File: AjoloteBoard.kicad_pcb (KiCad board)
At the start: 2 copper layers, 69 x 84.9 mm, 10 parts, among them SW1 SW_Push_SPDT

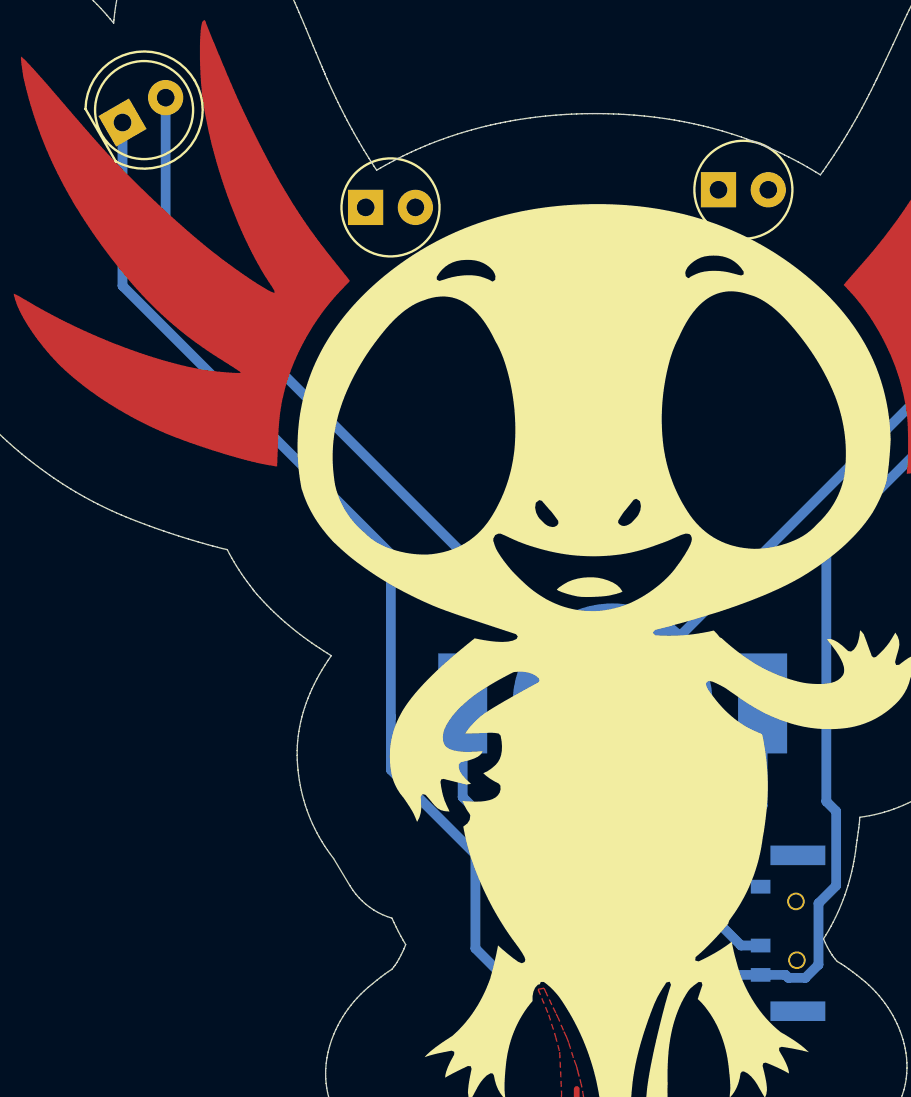
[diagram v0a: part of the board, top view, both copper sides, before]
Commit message: Update kicad version
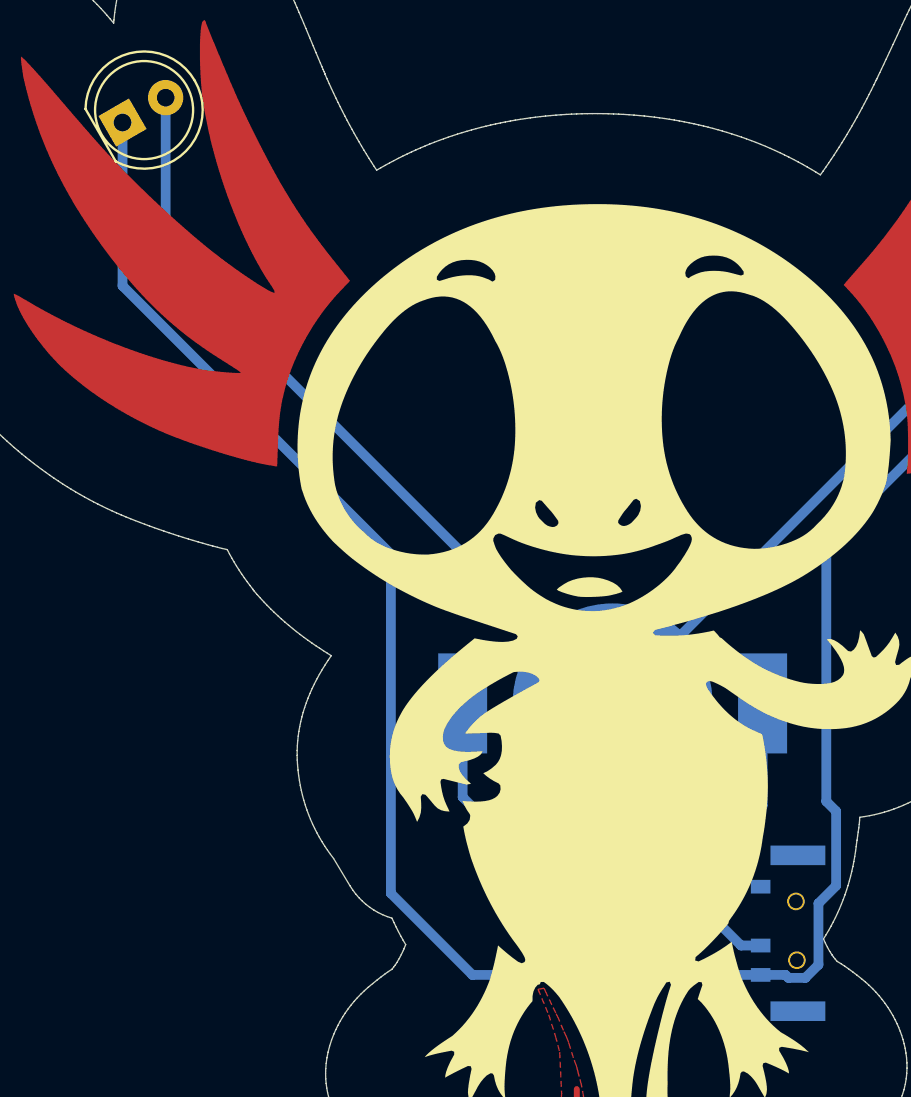
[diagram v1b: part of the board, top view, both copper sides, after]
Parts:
- removed the D1 at (147.2, 70.0)
- removed the D2 at (165.2, 69.1)
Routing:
- net Net-(D1-Pad1): track 116.7 -> 117.6 mm
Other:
- board text removed: "+"
- board text removed: "-"
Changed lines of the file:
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@@
-(kicad_pcb (version 4) (host pcbnew 4.0.7)
+(kicad_pcb (version 20171130) (host pcbnew "(5.0.0-3-g5ebb6b6)")
   (general
-    (links 0)
-    (no_connects 0)
-    (area 0 0 0 0)
     (thickness 1.6)
     (drawings 3)
-    (tracks 84)
+    (tracks 81)
     (zones 0)
     (modules 8)
@@
     (43 Eco2.User user)
     (44 Edge.Cuts user)
-    (45 Margin user hide)
+    (45 Margin user)
     (46 B.CrtYd user)
     (47 F.CrtYd user)
@@
       (layerselection 0x010f0_80000001)
       (usegerberextensions true)
+      (usegerberattributes false)
+      (usegerberadvancedattributes false)
+      (creategerberjobfile false)
       (excludeedgelayer true)
       (linewidth 0.100000)
@@
       (hpglpennumber 1)
       (hpglpenspeed 20)
-      (hpglpendiameter 15)
-      (hpglpenoverlay 2)
+      (hpglpendiameter 15.000000)
       (psnegative false)
       (psa4output false)
@@
       (drillshape 0)
       (scaleselection 1)
-      (outputdirectory /Volumes/Macintosh_HD/Documents/Electronic_Cats/Proyectos/Hw/WiFiTracker/AjoloteBoard/gerber/))
+      (outputdirectory "/Volumes/Macintosh_HD/Documents/Electronic_Cats/Proyectos/Hw/WiFiTracker/AjoloteBoard/gerber/"))
   )
   (net 0 "")
@@
     (add_net "Net-(SW1-Pad1)")
   )
-  (module LEDs:LED_D5.0mm (layer F.Cu)
-    (at 165.2 69.1)
-    (descr "LED, diameter 5.0mm, 2 pins, http://cdn-reichelt.de/documents/datenblatt/A500/LL-504BC2E-009.pdf")
-    (tags "LED diameter 5.0mm 2 pins")
-    (fp_text reference D2 (at 0.09 2.43) (layer B.SilkS)
-      (effects (font (size 1 1) (thickness 0.15)) (justify mirror))
-    )
-    (fp_text value LED (at 1.27 3.96) (layer F.Fab)
-      (effects (font (size 1 1) (thickness 0.15)))
-    )
-    (fp_arc (start 1.27 0) (end -1.23 -1.469694) (angle 299.1) (layer F.Fab) (width 0.1))
-    (fp_arc (start 1.27 0) (end -1.29 -1.54483) (angle 148.9) (layer F.Fab) (width 0.12))
-    (fp_arc (start 1.27 0) (end -1.29 1.54483) (angle -148.9) (layer F.Fab) (width 0.12))
-    (fp_circle (center 1.27 0) (end 3.77 0) (layer F.Fab) (width 0.1))
-    (fp_circle (center 1.27 0) (end 3.77 0) (layer F.SilkS) (width 0.12))
-    (fp_line (start -1.23 -1.469694) (end -1.23 1.469694) (layer F.Fab) (width 0.1))
-    (fp_line (start -1.29 -1.545) (end -1.29 1.545) (layer F.Fab) (width 0.12))
-    (fp_line (start -1.95 -3.25) (end -1.95 3.25) (layer F.CrtYd) (width 0.05))
-    (fp_line (start -1.95 3.25) (end 4.5 3.25) (layer F.CrtYd) (width 0.05))
-    (fp_line (start 4.5 3.25) (end 4.5 -3.25) (layer F.CrtYd) (width 0.05))
-    (fp_line (start 4.5 -3.25) (end -1.95 -3.25) (layer F.CrtYd) (width 0.05))
-    (fp_text user %R (at 1.25 0) (layer F.Fab)
-      (effects (font (size 0.8 0.8) (thickness 0.2)))
-    )
-    (pad 1 thru_hole rect (at 0 0) (size 1.8 1.8) (drill 0.9) (layers *.Cu *.Mask)
-      (net 2 "Net-(D1-Pad1)"))
-    (pad 2 thru_hole circle (at 2.54 0) (size 1.8 1.8) (drill 0.9) (layers *.Cu *.Mask)
-      (net 1 "Net-(BT1-Pad1)"))
-    (model ${KISYS3DMOD}/LEDs.3dshapes/LED_D5.0mm.wrl
-      (at (xyz 0 0 0))
-      (scale (xyz 0.393701 0.393701 0.393701))
-      (rotate (xyz 0 0 0))
-    )
-  )
-  (module LEDs:LED_D5.0mm (layer F.Cu)
-    (at 147.2 70)
-    (descr "LED, diameter 5.0mm, 2 pins, http://cdn-reichelt.de/documents/datenblatt/A500/LL-504BC2E-009.pdf")
-    (tags "LED diameter 5.0mm 2 pins")
-    (fp_text reference D1 (at 1.36 3.87) (layer B.SilkS)
-      (effects (font (size 1 1) (thickness 0.15)) (justify mirror))
-    )
-    (fp_text value LED (at 1.27 3.96) (layer F.Fab)
-      (effects (font (size 1 1) (thickness 0.15)))
-    )
-    (fp_arc (start 1.27 0) (end -1.23 -1.469694) (angle 299.1) (layer F.Fab) (width 0.1))
-    (fp_arc (start 1.27 0) (end -1.29 -1.54483) (angle 148.9) (layer F.Fab) (width 0.12))
-    (fp_arc (start 1.27 0) (end -1.29 1.54483) (angle -148.9) (layer F.Fab) (width 0.12))
-    (fp_circle (center 1.27 0) (end 3.77 0) (layer F.Fab) (width 0.1))
-    (fp_circle (center 1.27 0) (end 3.77 0) (layer F.SilkS) (width 0.12))
-    (fp_line (start -1.23 -1.469694) (end -1.23 1.469694) (layer F.Fab) (width 0.1))
-    (fp_line (start -1.29 -1.545) (end -1.29 1.545) (layer F.Fab) (width 0.12))
-    (fp_line (start -1.95 -3.25) (end -1.95 3.25) (layer F.CrtYd) (width 0.05))
-    (fp_line (start -1.95 3.25) (end 4.5 3.25) (layer F.CrtYd) (width 0.05))
-    (fp_line (start 4.5 3.25) (end 4.5 -3.25) (layer F.CrtYd) (width 0.05))
-    (fp_line (start 4.5 -3.25) (end -1.95 -3.25) (layer F.CrtYd) (width 0.05))
-    (fp_text user %R (at 1.25 0) (layer F.Fab)
-      (effects (font (size 0.8 0.8) (thickness 0.2)))
-    )
-    (pad 1 thru_hole rect (at 0 0) (size 1.8 1.8) (drill 0.9) (layers *.Cu *.Mask)
-      (net 2 "Net-(D1-Pad1)"))
-    (pad 2 thru_hole circle (at 2.54 0) (size 1.8 1.8) (drill 0.9) (layers *.Cu *.Mask)
-      (net 1 "Net-(BT1-Pad1)"))
-    (model ${KISYS3DMOD}/LEDs.3dshapes/LED_D5.0mm.wrl
-      (at (xyz 0 0 0))
-      (scale (xyz 0.393701 0.393701 0.393701))
-      (rotate (xyz 0 0 0))
-    )
-  )
   (module svg2mod (layer F.Cu)
     (at 165.48 97.94)
@@
     (attr smd)
     (fp_text reference svg2mod (at 0 -45.573156) (layer F.SilkS) hide
-      (effects (font (thickness 0.3048)))
+      (effects (font (size 1.524 1.524) (thickness 0.3048)))
     )
     (fp_text value ajolote (at 0 45.573156) (layer F.SilkS) hide
-      (effects (font (thickness 0.3048)))
+      (effects (font (size 1.524 1.524) (thickness 0.3048)))
     )
     (fp_poly (pts (xy -14.515576 -24.189531) (xy -21.400934 -18.448258) (xy -21.335838 -18.680274) (xy -21.265249 -18.910624)
@@
     (at 179.75 73.93 180)
     (fp_text reference G*** (at 0 0 180) (layer B.SilkS) hide
-      (effects (font (thickness 0.3)) (justify mirror))
+      (effects (font (size 1.524 1.524) (thickness 0.3)) (justify mirror))
     )
     (fp_text value LOGO (at 0.75 0 180) (layer B.SilkS) hide
-      (effects (font (thickness 0.3)) (justify mirror))
+      (effects (font (size 1.524 1.524) (thickness 0.3)) (justify mirror))
     )
     (fp_poly (pts (xy -1.511952 -2.134469) (xy -1.457322 -2.134584) (xy -1.408721 -2.134798) (xy -1.367028 -2.135106)
@@
       (xy 1.530863 2.420002) (xy 1.583231 2.473048) (xy 2.125049 3.022233) (xy 2.12443 2.935152)) (layer B.SilkS) (width 0.01))
   )
-  (gr_text - (at 170.41 68.86) (layer B.SilkS)
-    (effects (font (size 1.5 1.5) (thickness 0.3)))
-  )
-  (gr_text + (at 163.07 69.08) (layer B.SilkS)
-    (effects (font (size 1.5 1.5) (thickness 0.3)))
-  )
-  (gr_text - (at 152.45 69.94) (layer B.SilkS)
-    (effects (font (size 1.5 1.5) (thickness 0.3)))
-  )
-  (gr_text + (at 144.97 69.85) (layer B.SilkS)
-    (effects (font (size 1.5 1.5) (thickness 0.3)))
-  )
-  (gr_text "Thanks for you help Axolote" (at 159.6 120.43 90) (layer B.SilkS)
-    (effects (font (size 1.5 1.5) (thickness 0.25) italic) (justify mirror))
+  (gr_text "Thanks for you help Axolote" (at 159.97 120.52 90) (layer B.SilkS)
+    (effects (font (size 1.5 1) (thickness 0.25) italic) (justify mirror))
   )
   (dimension 69.107236 (width 0.3) (layer Margin)
@@
   (segment (start 159.8 95.3) (end 181.213181 73.886819) (width 0.5) (layer B.Cu) (net 1))
   (segment (start 181.213181 73.886819) (end 181.213181 64.931269) (width 0.5) (layer B.Cu) (net 1))
-  (segment (start 148.489999 87.689999) (end 148.489999 96) (width 0.5) (layer B.Cu) (net 2))
-  (segment (start 152.8 103) (end 148.489999 98.689999) (width 0.5) (layer B.Cu) (net 2))
-  (segment (start 167.35 109.15) (end 154.15 109.15) (width 0.5) (layer B.Cu) (net 2))
-  (segment (start 154.15 109.15) (end 152.8 107.8) (width 0.5) (layer B.Cu) (net 2))
-  (segment (start 152.8 107.8) (end 152.8 103) (width 0.5) (layer B.Cu) (net 2))
-  (segment (start 148.489999 98.689999) (end 148.489999 96) (width 0.5) (layer B.Cu) (net 2))
   (segment (start 170.7 100.3) (end 170.7 87.6) (width 0.5) (layer B.Cu) (net 2))
   (segment (start 170.7 87.6) (end 170.7 87.1) (width 0.5) (layer B.Cu) (net 2))
@@
   (segment (start 168.617998 109.15) (end 168.767999 109.300001) (width 0.5) (layer B.Cu) (net 2))
   (segment (start 168.767999 109.300001) (end 169.632001 109.300001) (width 0.5) (layer B.Cu) (net 2))
-  (segment (start 134.800295 74.000295) (end 148.489999 87.689999) (width 0.5) (layer B.Cu) (net 2))
-  (segment (start 134.800295 65.67) (end 134.800295 74.000295) (width 0.5) (layer B.Cu) (net 2))
+  (segment (start 134.800295 74.000295) (end 134.800295 65.67) (width 0.5) (layer B.Cu) (net 2))
+  (segment (start 148.489999 87.689999) (end 134.800295 74.000295) (width 0.5) (layer B.Cu) (net 2))
+  (segment (start 148.489999 104.989999) (end 148.489999 87.689999) (width 0.5) (layer B.Cu) (net 2))
+  (segment (start 152.65 109.15) (end 148.489999 104.989999) (width 0.5) (layer B.Cu) (net 2))
+  (segment (start 167.35 109.15) (end 152.65 109.15) (width 0.5) (layer B.Cu) (net 2))
   (segment (start 166.116 101.854) (end 165.5 101.854) (width 0.5) (layer B.Cu) (net 3))
   (segment (start 165.5 101.854) (end 164.2 101.854) (width 0.5) (layer B.Cu) (net 3))

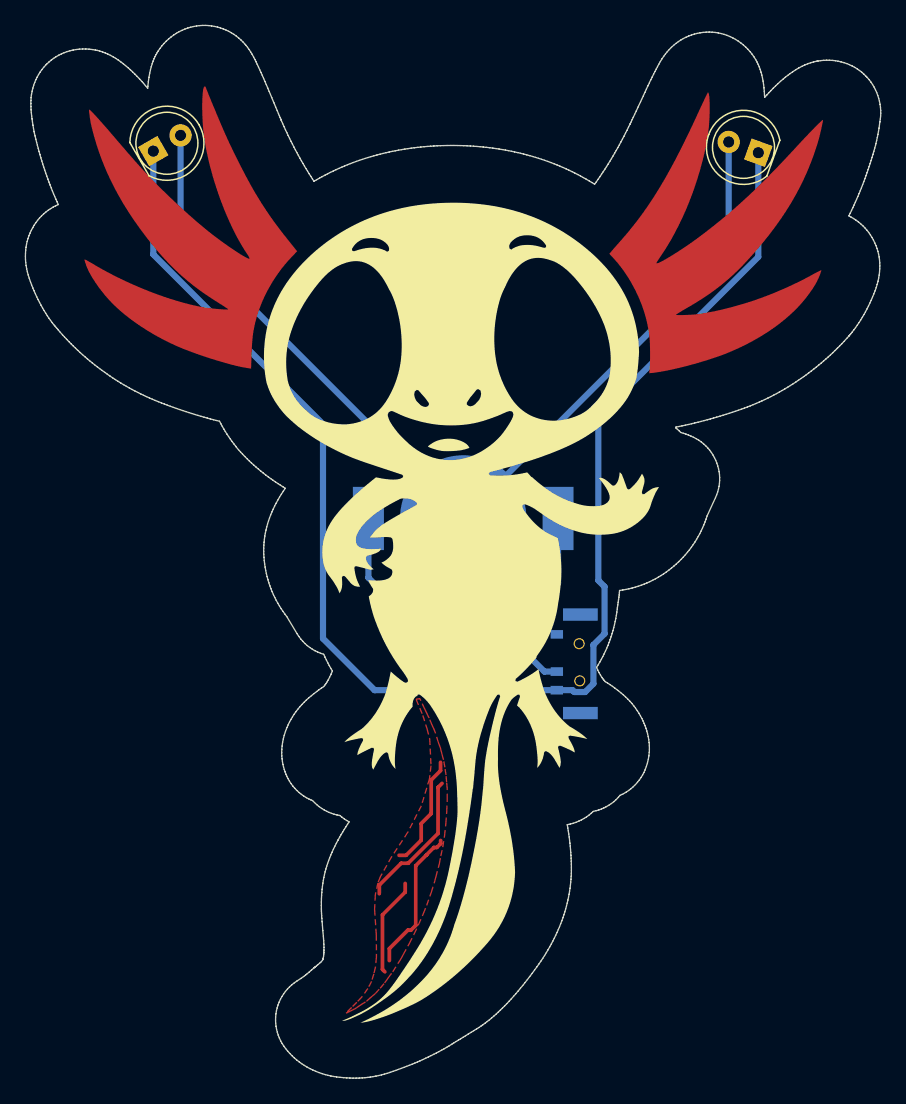
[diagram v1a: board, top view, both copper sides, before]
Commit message: fix inverted leds
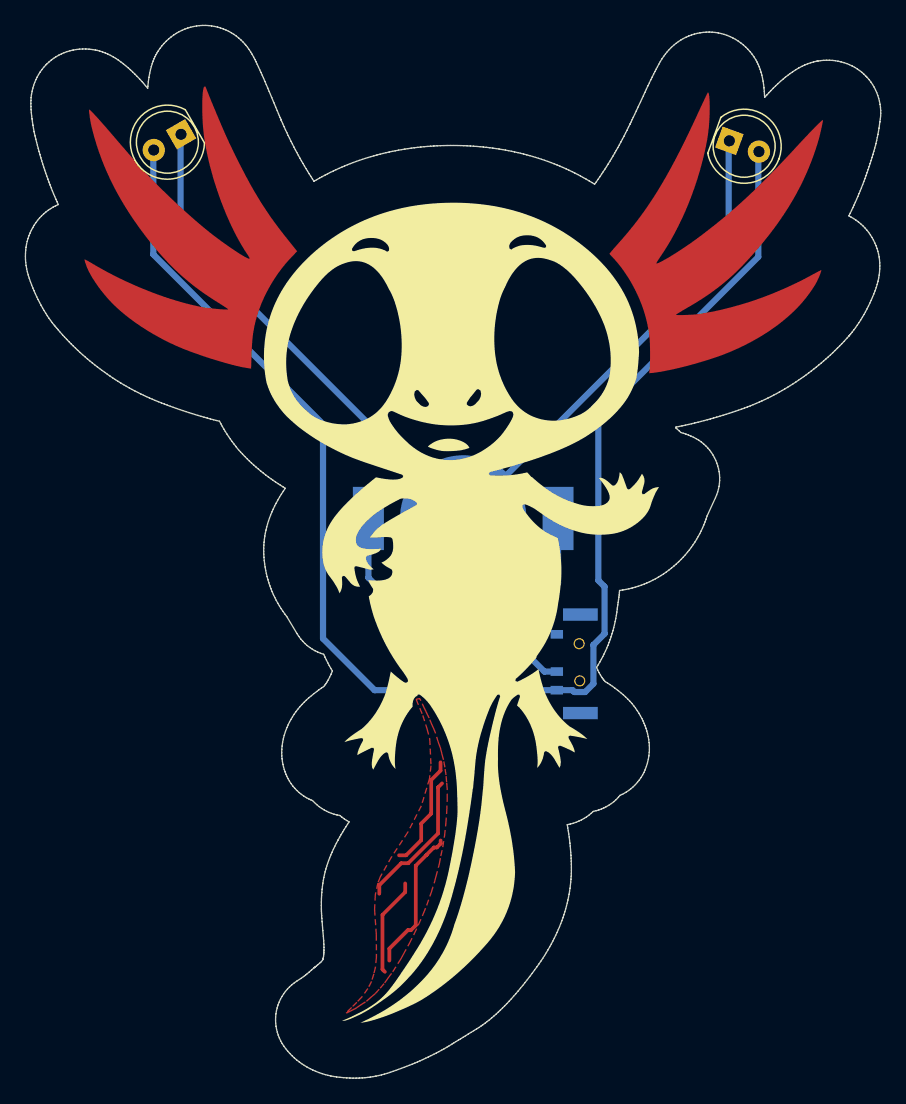
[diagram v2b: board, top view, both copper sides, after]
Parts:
- moved D1 2.62 mm to (137.0, 64.3), turned to 210 degrees
- moved D2 2.52 mm to (181.3, 64.8), turned to 340 degrees
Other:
- board text added: "Axolote Board"
- board text added: "electroniccats.com"
- board text added: "v0.2"

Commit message: Update foorprints and floor plan
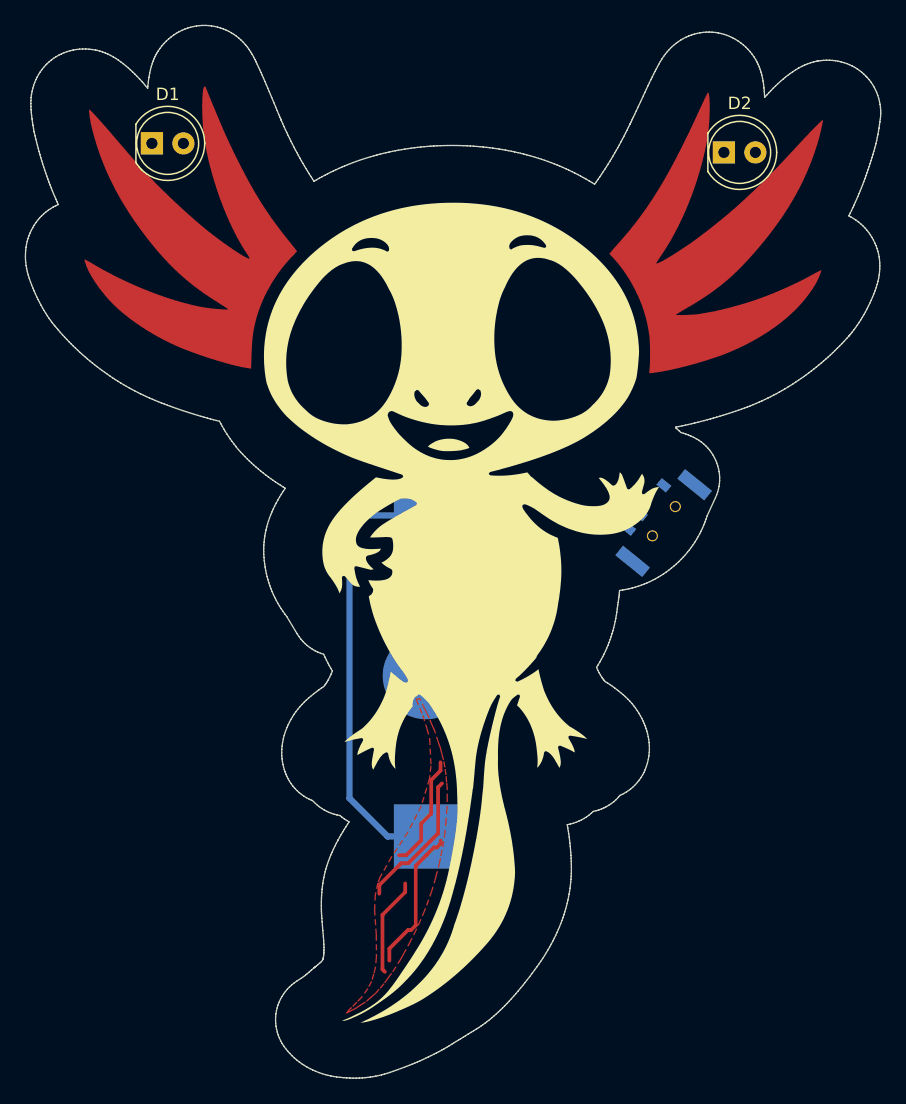
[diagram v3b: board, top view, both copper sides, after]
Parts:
- removed Battery: Battery_Cell, Batteries:BAT-HLD-012-SMT-OTL
- added BT1: Battery_Cell, footprints:79523141, B.Cu at (156.8, 108.0)
- D1, D2: footprint LEDs:LED_D5.0mm -> LED_THT:LED_D5.0mm_Clear
- SW1: value SW_Push_SPDT -> On; footprint Micro_interruptor_SPDT -> footprints:Micro_interruptor_SPDT
- moved SW1 13.1 mm to (179.4, 93.5), turned to 141 degrees
- moved D1 2.46 mm to (134.7, 65.0), turned to 0 degrees
- moved D2 1.03 mm to (180.8, 65.8), turned to 0 degrees
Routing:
- net Net-(D1-Pad1): track 117.6 -> 0.00 mm
- net Net-(BT1-Pad2): track 58.9 -> 0.00 mm
- net Net-(BT1-Pad1): track 79.6 -> 35.8 mm
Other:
- net class Default: clearance 0.2 -> 0.35
- rule trace_clearance: 0.2 -> 0.35
- board text added: "v0.3"
- board text removed: "v0.2"

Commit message: update to v0.3
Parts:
- moved REF*** 58.6 mm to (154.4, 130.0)
- moved SW1 1.52 mm to (178.1, 92.7)
- moved D2 0.77 mm to (180.8, 65.0)
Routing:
- net Net-(D1-Pad1): track 0.00 -> 125.4 mm
- net Net-(BT1-Pad1): track 35.8 -> 141.4 mm
- net Net-(BT1-Pad2): track 0.00 -> 26.2 mm

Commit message: Add logos wurth
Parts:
- added G***: LOGO, Aesthetics:wurth, B.Cu at (136.9, 75.7)
- added svg2mod: G***, Aesthetics:heart, B.Cu at (158.8, 88.8)
